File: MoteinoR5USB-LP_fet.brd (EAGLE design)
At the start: 44.7 x 23.1 mm, 34 parts, among them CN1 MINIB, IC3 MCP1703CB, U1 FT231XS, U3 SN74LVC1T45, X1 16 MHz

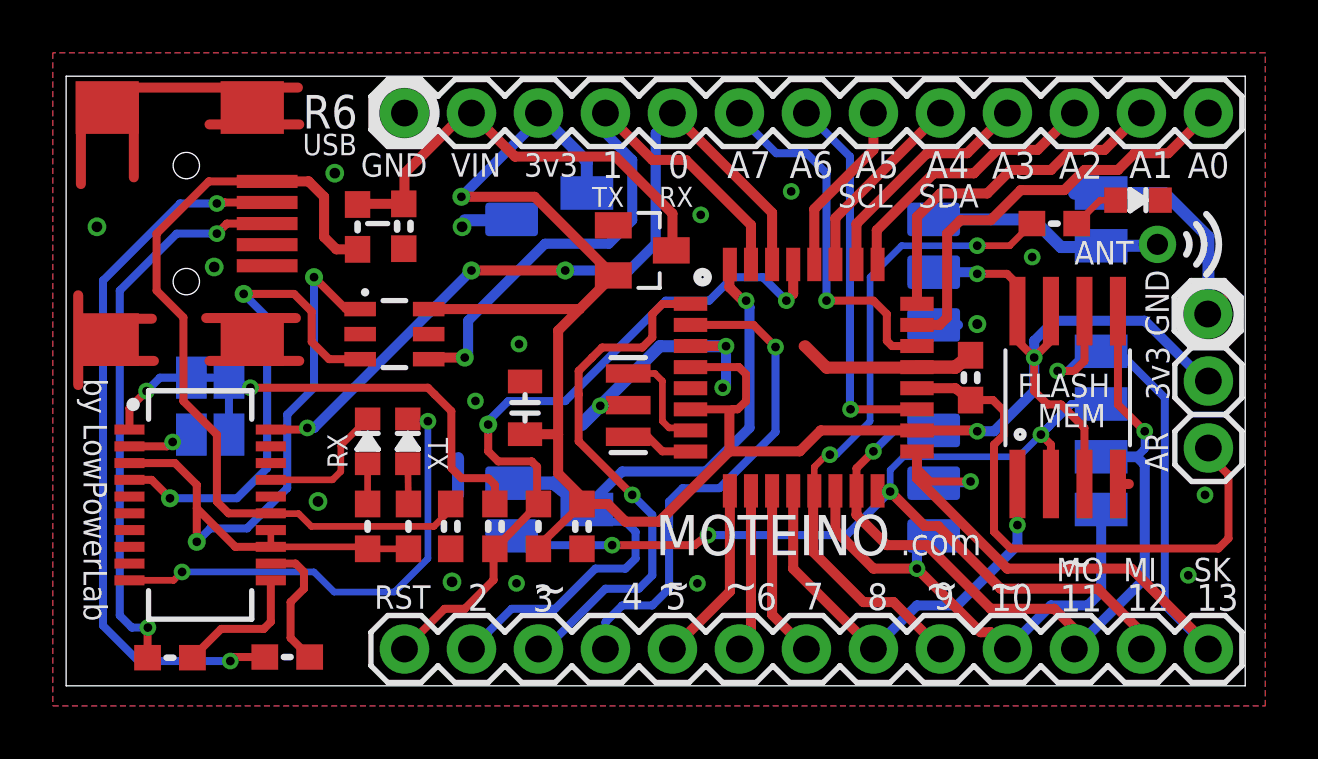
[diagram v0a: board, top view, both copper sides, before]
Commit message: Added a MOSFET variant
- replaced voltage shifter with mosfet
- some trace & silkscreen adjustments on both boards
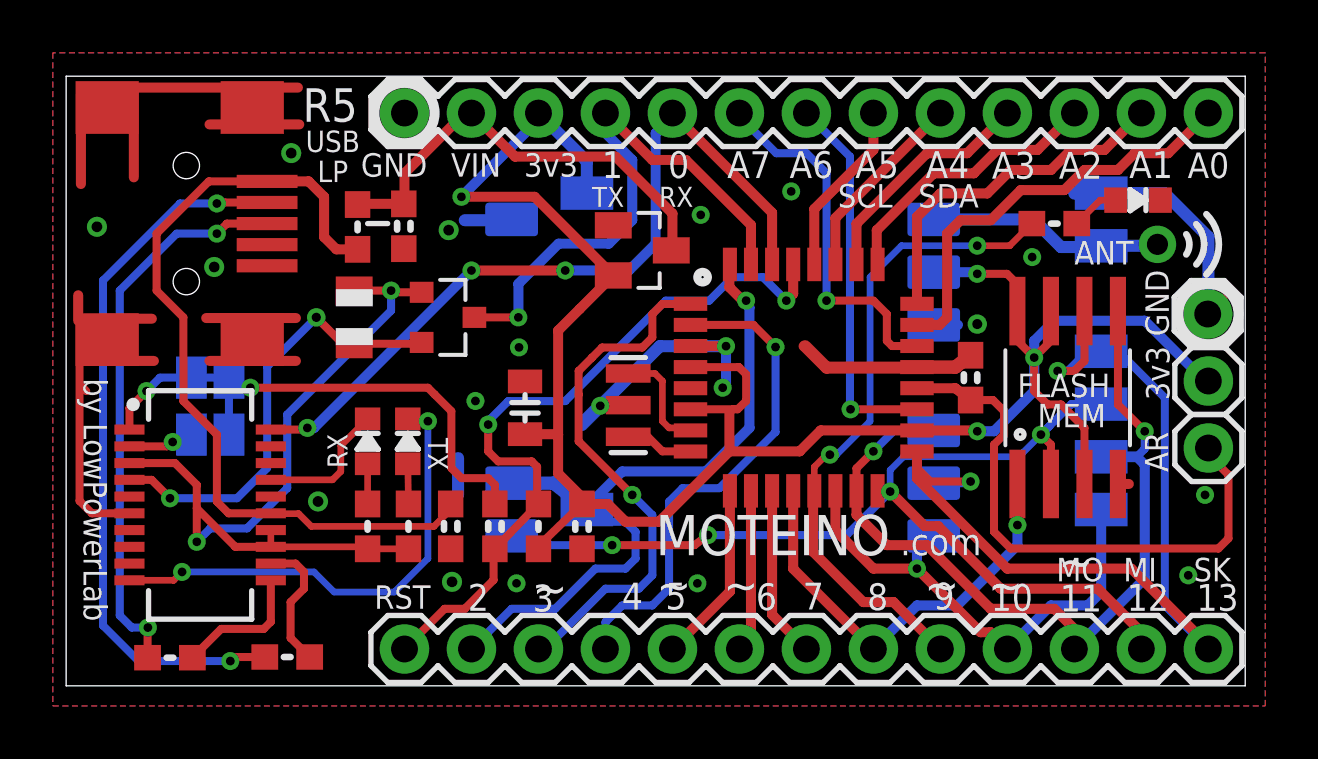
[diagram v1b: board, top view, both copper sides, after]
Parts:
- removed U3: SN74LVC1T45, SN74LVC1T45:SOT23-6
- added R7: 10K, adafruit:R0805
- added U$8: N-CHANNEL-MOSFET-BSS138, GeekAmmo:SOT23-3
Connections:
- net D1_TX: now also U$8.3; no longer U3.4
- net FTDI3.3V: now also R7.1, U$8.1; no longer U3.1
- net FTDI_RX: now also R7.2, U$8.2; no longer U3.3
- net GND: no longer U3.2, U3.5
- net VCC: no longer U3.6
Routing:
- net GND: track 64.9 -> 72.9 mm
- net VCC: track 85.7 -> 79.9 mm
- net D1_TX: track 23.9 -> 21.5 mm
- net FTDI_RX: track 19.1 -> 16.9 mm
- net FTDI3.3V: track 29.3 -> 30.4 mm
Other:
- board text added: "R5"
- board text added: "USB LP"
- board text removed: "R6"
- board text removed: "USB"
